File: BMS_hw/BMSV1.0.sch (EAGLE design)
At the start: 181 parts, among them IC1 MC33771BEP, IC2 SFH6156, IC3 MIC28515V1, J2 NTC, X2 87758-1816

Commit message: push_2
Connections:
- removed net CS: IC1.CSB
- removed net N$14: C9.1, R7.2, R8.2
- net GND: now also C9.1, R7.2, R8.2
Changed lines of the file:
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@@
 <part name="R7" library="simpa" deviceset="WSR3R0150FEA" device=""/>
 <part name="R8" library="simpa" deviceset="WSR3R0150FEA" device=""/>
-<part name="GND16" library="supply1" library_urn="urn:adsk.eagle:library:371" deviceset="GND" device=""/>
 <part name="GND17" library="supply1" library_urn="urn:adsk.eagle:library:371" deviceset="GND" device=""/>
-<part name="GND22" library="supply1" library_urn="urn:adsk.eagle:library:371" deviceset="GND" device=""/>
 <part name="PACKV-" library="supply2" library_urn="urn:adsk.eagle:library:372" deviceset="V-" device=""/>
 <part name="P-2" library="supply2" library_urn="urn:adsk.eagle:library:372" deviceset="V-" device=""/>
@@
 <wire x1="365.76" y1="73.66" x2="365.76" y2="109.22" width="0.1524" layer="91"/>
 <wire x1="365.76" y1="109.22" x2="299.72" y2="109.22" width="0.1524" layer="91"/>
-</segment>
-</net>
-<net name="CS" class="0">
-<segment>
-<pinref part="IC1" gate="G$1" pin="CSB"/>
-<wire x1="243.84" y1="83.82" x2="241.3" y2="83.82" width="0.1524" layer="91"/>
-<label x="243.84" y="83.82" size="1.778" layer="95" xref="yes"/>
 </segment>
 </net>
@@
 <attribute name="NAME" x="288.036" y="218.44" size="1.778" layer="95" rot="R90"/>
 </instance>
-<instance part="GND16" gate="1" x="256.54" y="226.06"/>
 <instance part="GND17" gate="1" x="271.78" y="226.06"/>
-<instance part="GND22" gate="1" x="264.16" y="226.06"/>
 <instance part="PACKV-" gate="1" x="256.54" y="200.66"/>
 <instance part="P-2" gate="1" x="264.16" y="200.66"/>
@@
 <wire x1="340.36" y1="99.06" x2="340.36" y2="114.3" width="0.1524" layer="91"/>
 <junction x="340.36" y="114.3"/>
+</segment>
+<segment>
+<pinref part="R7" gate="G$1" pin="2"/>
+<wire x1="281.94" y1="226.06" x2="281.94" y2="231.14" width="0.1524" layer="91"/>
+<wire x1="279.4" y1="231.14" x2="281.94" y2="231.14" width="0.1524" layer="91"/>
+<pinref part="GND17" gate="1" pin="GND"/>
+<wire x1="271.78" y1="228.6" x2="271.796" y2="231.14" width="0.1524" layer="91"/>
+<wire x1="271.796" y1="231.14" x2="276.86" y2="231.14" width="0.1524" layer="91"/>
+<wire x1="276.86" y1="231.14" x2="279.4" y2="231.14" width="0.1524" layer="91"/>
+<wire x1="289.56" y1="236.22" x2="289.56" y2="233.68" width="0.1524" layer="91"/>
+<pinref part="R8" gate="G$1" pin="2"/>
+<wire x1="289.56" y1="226.06" x2="289.56" y2="231.14" width="0.1524" layer="91"/>
+<wire x1="289.56" y1="231.14" x2="289.56" y2="233.68" width="0.1524" layer="91"/>
+<pinref part="C9" gate="G$1" pin="1"/>
+<wire x1="302.26" y1="238.76" x2="302.26" y2="231.14" width="0.1524" layer="91"/>
+<wire x1="302.26" y1="238.76" x2="289.56" y2="238.76" width="0.1524" layer="91"/>
+<wire x1="289.56" y1="236.22" x2="289.56" y2="238.76" width="0.1524" layer="91"/>
+<wire x1="281.94" y1="231.14" x2="289.56" y2="231.14" width="0.1524" layer="91"/>
+<junction x="281.94" y="231.14"/>
+<junction x="289.56" y="231.14"/>
 </segment>
 </net>
@@
 </segment>
 </net>
-<net name="N$14" class="0">
-<segment>
-<pinref part="GND22" gate="1" pin="GND"/>
-<wire x1="264.16" y1="228.6" x2="264.16" y2="228.498" width="0.1524" layer="91"/>
-<wire x1="264.16" y1="228.498" x2="264.16" y2="233.68" width="0.1524" layer="91"/>
-<pinref part="R7" gate="G$1" pin="2"/>
-<wire x1="281.94" y1="226.06" x2="281.94" y2="231.14" width="0.1524" layer="91"/>
-<pinref part="GND16" gate="1" pin="GND"/>
-<wire x1="281.94" y1="231.14" x2="281.94" y2="233.68" width="0.1524" layer="91"/>
-<wire x1="281.94" y1="233.68" x2="281.94" y2="236.22" width="0.1524" layer="91"/>
-<wire x1="281.94" y1="236.22" x2="281.94" y2="238.76" width="0.1524" layer="91"/>
-<wire x1="256.54" y1="228.6" x2="256.54" y2="236.22" width="0.1524" layer="91"/>
-<wire x1="256.54" y1="236.22" x2="274.32" y2="236.22" width="0.1524" layer="91"/>
-<junction x="281.94" y="236.22"/>
-<pinref part="GND17" gate="1" pin="GND"/>
-<wire x1="274.32" y1="236.22" x2="276.86" y2="236.22" width="0.1524" layer="91"/>
-<wire x1="276.86" y1="236.22" x2="279.4" y2="236.22" width="0.1524" layer="91"/>
-<wire x1="279.4" y1="236.22" x2="281.94" y2="236.22" width="0.1524" layer="91"/>
-<wire x1="271.78" y1="228.6" x2="271.796" y2="231.14" width="0.1524" layer="91"/>
-<wire x1="271.796" y1="231.14" x2="276.86" y2="231.14" width="0.1524" layer="91"/>
-<junction x="289.56" y="231.14"/>
-<wire x1="276.86" y1="231.14" x2="279.4" y2="231.14" width="0.1524" layer="91"/>
-<wire x1="279.4" y1="231.14" x2="281.94" y2="231.14" width="0.1524" layer="91"/>
-<wire x1="281.94" y1="231.14" x2="289.56" y2="231.14" width="0.1524" layer="91"/>
-<wire x1="276.86" y1="236.22" x2="276.86" y2="233.68" width="0.1524" layer="91"/>
-<junction x="276.86" y="236.22"/>
-<junction x="276.86" y="231.14"/>
-<wire x1="276.86" y1="233.68" x2="276.86" y2="231.14" width="0.1524" layer="91"/>
-<wire x1="279.4" y1="236.22" x2="279.4" y2="233.68" width="0.1524" layer="91"/>
-<junction x="279.4" y="236.22"/>
-<junction x="279.4" y="231.14"/>
-<wire x1="279.4" y1="233.68" x2="279.4" y2="231.14" width="0.1524" layer="91"/>
-<wire x1="281.94" y1="236.22" x2="289.56" y2="236.22" width="0.1524" layer="91"/>
-<wire x1="289.56" y1="236.22" x2="289.56" y2="233.68" width="0.1524" layer="91"/>
-<wire x1="289.56" y1="233.68" x2="281.94" y2="233.68" width="0.1524" layer="91"/>
-<junction x="281.94" y="233.68"/>
-<junction x="289.56" y="233.68"/>
-<junction x="289.56" y="236.22"/>
-<wire x1="274.32" y1="236.22" x2="274.32" y2="233.68" width="0.1524" layer="91"/>
-<junction x="274.32" y="236.22"/>
-<junction x="274.32" y="231.14"/>
-<wire x1="274.32" y1="233.68" x2="274.32" y2="231.14" width="0.1524" layer="91"/>
-<wire x1="264.16" y1="233.68" x2="274.32" y2="233.68" width="0.1524" layer="91"/>
-<junction x="274.32" y="233.68"/>
-<wire x1="274.32" y1="233.68" x2="276.86" y2="233.68" width="0.1524" layer="91"/>
-<junction x="276.86" y="233.68"/>
-<wire x1="276.86" y1="233.68" x2="279.4" y2="233.68" width="0.1524" layer="91"/>
-<junction x="279.4" y="233.68"/>
-<wire x1="279.4" y1="233.68" x2="281.94" y2="233.68" width="0.1524" layer="91"/>
-<junction x="281.94" y="231.14"/>
-<pinref part="R8" gate="G$1" pin="2"/>
-<wire x1="289.56" y1="226.06" x2="289.56" y2="231.14" width="0.1524" layer="91"/>
-<wire x1="289.56" y1="231.14" x2="289.56" y2="233.68" width="0.1524" layer="91"/>
-<pinref part="C9" gate="G$1" pin="1"/>
-<wire x1="302.26" y1="238.76" x2="302.26" y2="231.14" width="0.1524" layer="91"/>
-<wire x1="302.26" y1="238.76" x2="289.56" y2="238.76" width="0.1524" layer="91"/>
-<wire x1="289.56" y1="236.22" x2="289.56" y2="238.76" width="0.1524" layer="91"/>
-<wire x1="289.56" y1="238.76" x2="281.94" y2="238.76" width="0.1524" layer="91"/>
-<junction x="289.56" y="238.76"/>
-<wire x1="281.94" y1="238.76" x2="279.4" y2="238.76" width="0.1524" layer="91"/>
-<junction x="281.94" y="238.76"/>
-<label x="279.4" y="238.76" size="1.778" layer="95" rot="R180" xref="yes"/>
-</segment>
-</net>
 <net name="N$10" class="0">
 <segment>
@@
 </sheet>
 </sheets>
+<errors>
+</errors>
 </schematic>
 </drawing>

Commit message: push_3
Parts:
- added D1: 8.2v, diode:ZENER-DIODESOD80C
- added R29, R30: 10k, adafruit:R-US_R0805
- added T1, T2, T3, T4: IPT020N10N3V1, GreenFuel:IPT020N10N3V1
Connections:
- new net CHG_MOSFET: D1.C, R30.2, T1.G, T3.G
- new net DSG_MOSFET: R29.2, T2.G, T4.G
- new net N$29: T1.D, T1.D1, T1.D2, T2.D, T2.D1, T2.D2, T3.D, T3.D1, T3.D2, T4.D, T4.D1, T4.D2
- new net N$61: R29.1, T2.S, T2.S1, T2.S2, T2.S3, T2.S4, T2.S5, T2.S6, T4.S, T4.S1, T4.S2, T4.S3, T4.S4, T4.S5, T4.S6
- new net N$67: D1.A, R30.1, T1.S, T1.S1, T1.S2, T1.S3, T1.S4, T1.S5, T1.S6, T3.S, T3.S1, T3.S2, T3.S3, T3.S4, T3.S5, T3.S6

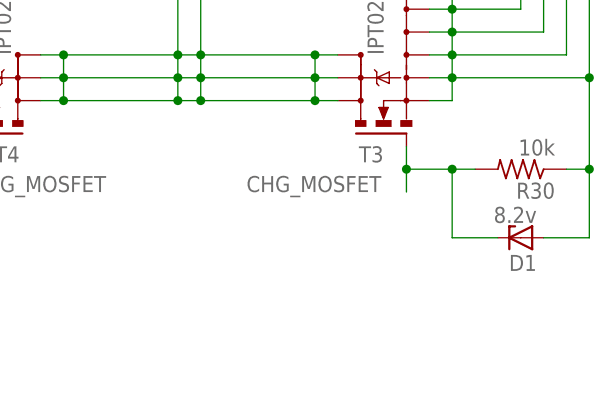
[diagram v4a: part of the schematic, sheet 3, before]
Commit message: gate pull up diode added in schematic and board
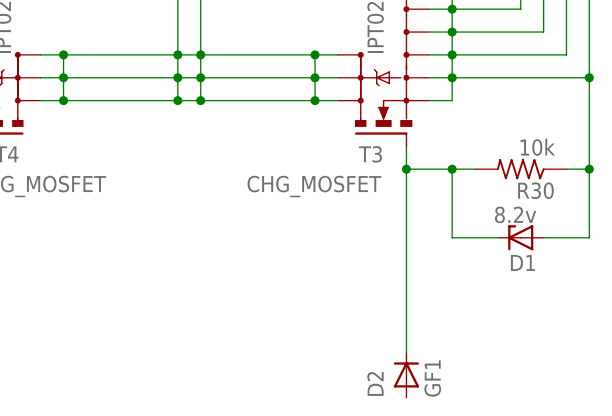
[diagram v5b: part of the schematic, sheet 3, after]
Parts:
- added D2: GF1, diode:GF1
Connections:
- net CHG_MOSFET: now also D2.C
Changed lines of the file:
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@@
 <setting verticaltext="up"/>
 </settings>
-<grid distance="0.1" unitdist="inch" unit="mil" style="lines" multiple="1" display="yes" altdistance="0.01" altunitdist="inch" altunit="mil"/>
+<grid distance="0.1" unitdist="inch" unit="mil" style="dots" multiple="1" display="yes" altdistance="0.01" altunitdist="inch" altunit="mil"/>
 <layers>
 <layer number="1" name="Top" color="4" fill="1" visible="no" active="no"/>
@@
 <part name="R30" library="adafruit" deviceset="R-US_" device="R0805" value="10k"/>
 <part name="D1" library="diode" library_urn="urn:adsk.eagle:library:210" deviceset="ZENER-DIODE" device="SOD80C" package3d_urn="urn:adsk.eagle:package:43405/2" value="8.2v"/>
+<part name="D2" library="diode" library_urn="urn:adsk.eagle:library:210" deviceset="GF1" device="" package3d_urn="urn:adsk.eagle:package:43452/2"/>
 </parts>
 <sheets>
@@
 <instance part="R30" gate="G$1" x="213.36" y="121.92" rot="R180"/>
 <instance part="D1" gate="G$1" x="213.36" y="114.3" rot="R180"/>
+<instance part="D2" gate="D" x="200.66" y="99.06" rot="R90"/>
 </instances>
 <busses>
@@
 <label x="182.88" y="119.38" size="1.778" layer="95"/>
 <pinref part="R30" gate="G$1" pin="2"/>
-<wire x1="200.66" y1="121.92" x2="200.66" y2="119.38" width="0.1524" layer="91"/>
 <wire x1="208.28" y1="121.92" x2="205.74" y2="121.92" width="0.1524" layer="91"/>
 <junction x="200.66" y="121.92"/>
@@
 <wire x1="205.74" y1="114.3" x2="205.74" y2="121.92" width="0.1524" layer="91"/>
 <junction x="205.74" y="121.92"/>
+<pinref part="D2" gate="D" pin="C"/>
+<wire x1="200.66" y1="101.6" x2="200.66" y2="121.92" width="0.1524" layer="91"/>
 </segment>
 </net>

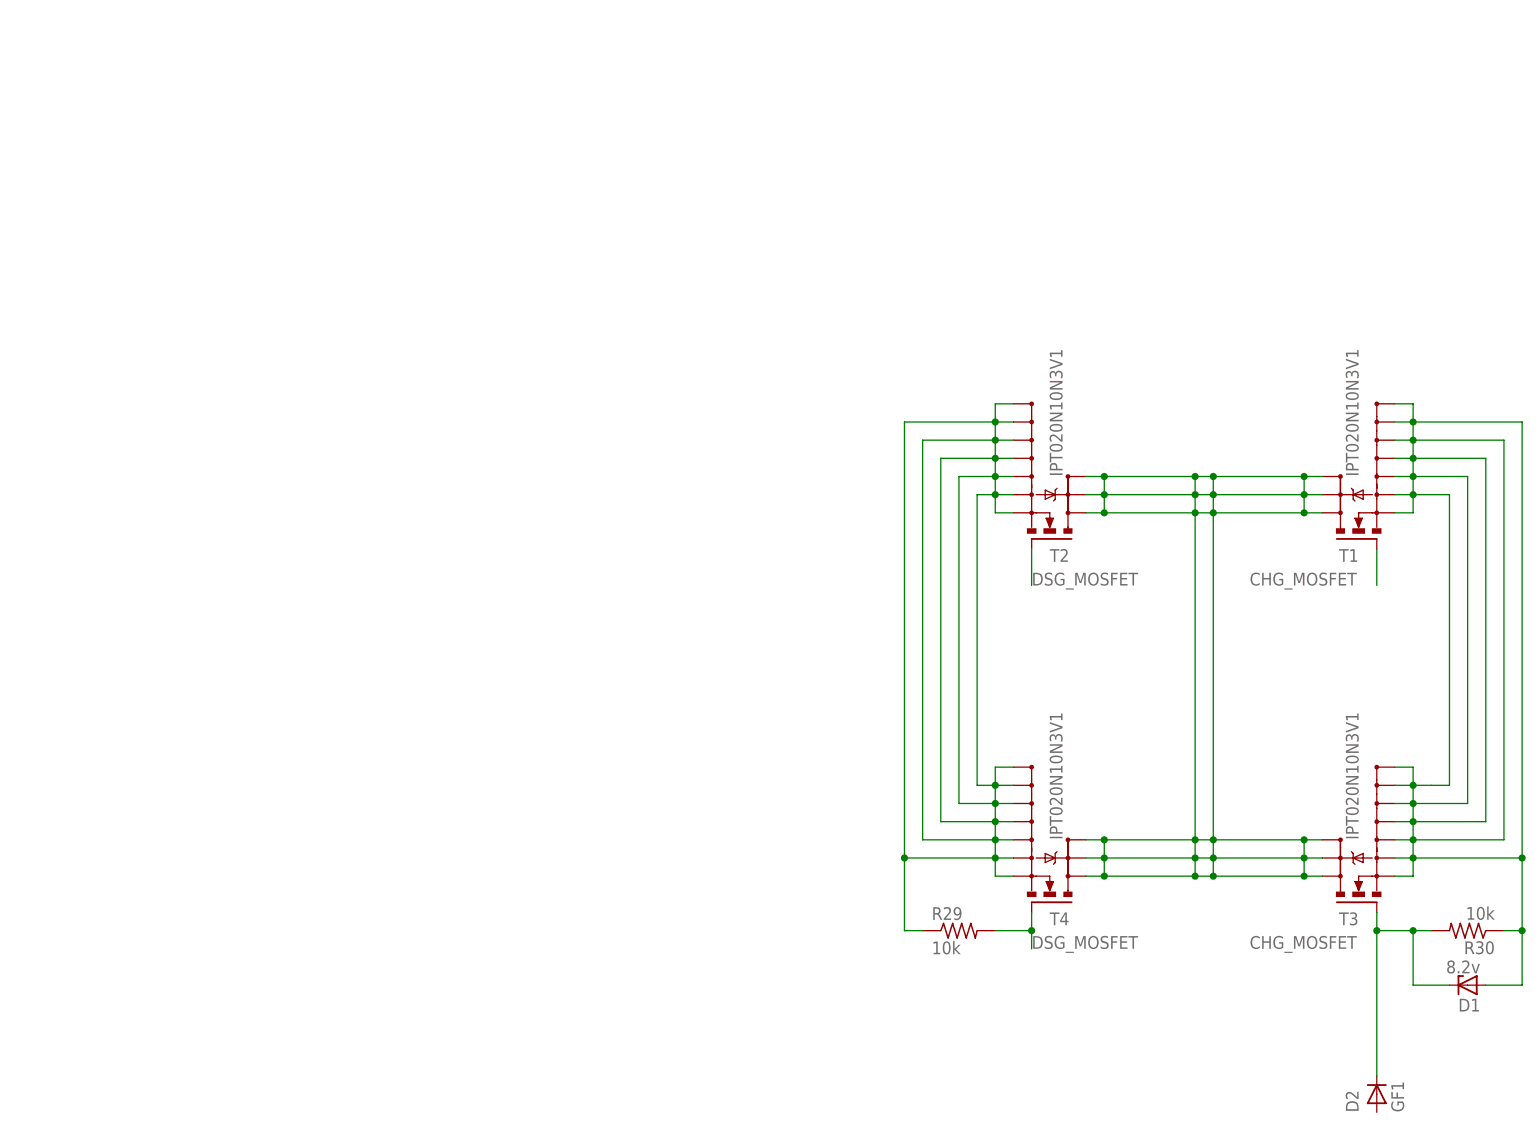
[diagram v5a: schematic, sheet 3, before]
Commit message: chg and dsg mosfet circuit final submission
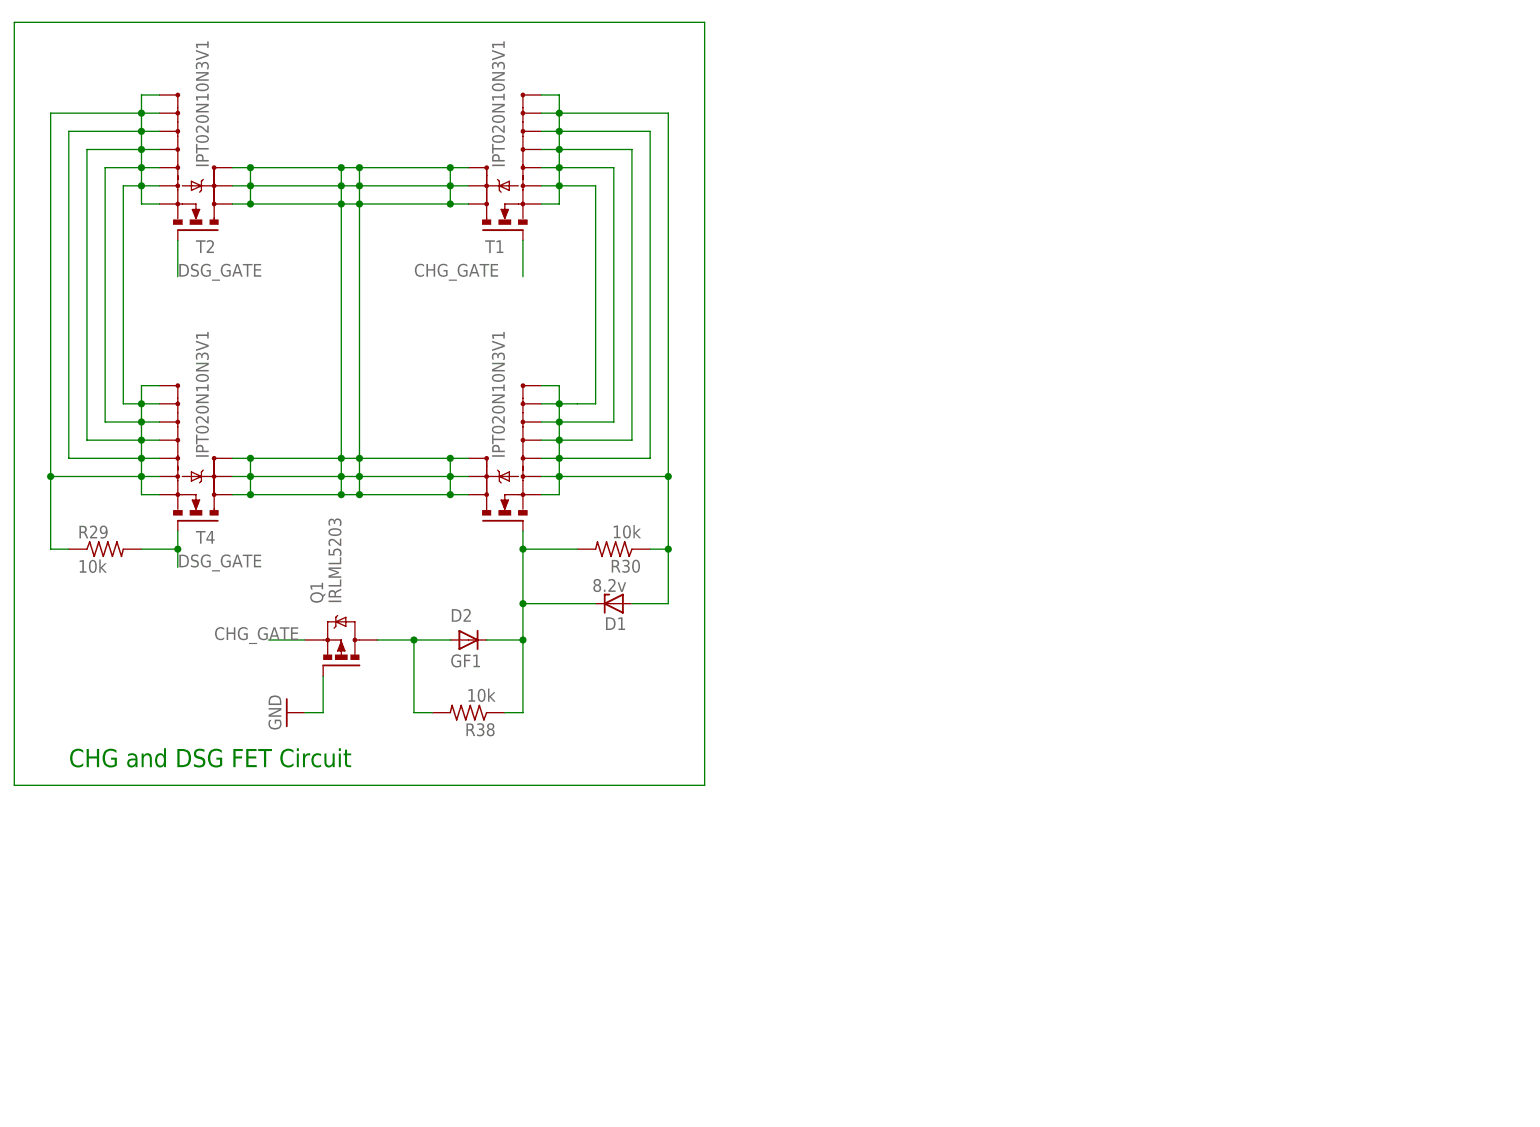
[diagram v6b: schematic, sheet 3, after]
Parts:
- added Q1: IRLML5203, transistor-power:IRLML5203
- added R38: 10k, adafruit:R-US_R0805
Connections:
- net DSG_MOSFET renamed DSG_GATE
- removed net CHG_MOSFET: D1.C, D2.C, R30.2, T1.G, T3.G
- new net CHG_GATE: Q1.S, T1.G
- new net N$19: D2.A, Q1.D, R38.2
- new net N$23: D1.C, D2.C, R30.2, R38.1, T3.G
- net GND: now also Q1.G
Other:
- note added: "CHG and DSG FET Circuit"
- moved on the sheet: D1, D2, R29, R30, T1, T2, T4
